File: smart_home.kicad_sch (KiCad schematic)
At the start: 0 parts

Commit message: Complete 4-channel smart home AC relay PCB design
Full KiCad 9 design for a 230V AC 4-channel smart home relay controller:
- ESP32-WROOM-32E + ULN2003A + 4x SANYOU SRD relays
- 4 isolated AC inputs (own L/N/PE + fuse per channel)
- 4 AC outputs (L_switched + N_passthrough per channel)
- HLK-PM01 isolated AC-DC + AMS1117-3.3 LDO for logic
- Per-channel current sense (4x ACS712-05B + ADC dividers)
- Per-channel voltage sense (ADS1115 I2C ADC + external ZMPT101B headers)
- 4-pin I2C header for 16x2 LCD module (PCF8574 backpack)
- Manual override buttons + status LEDs per channel
- 6-pin UART programming header
- Custom DRC: 4mm HV-LV clearance, 3mm HV-HV, 2mm HV trace minimum
- Physical HV/LV isolation slot in PCB

Layout: 200x100mm 2-layer FR4, 76 components, mostly routed (Freerouting).
21 HV channel-internal traces still need manual routing in KiCad.

Includes generator scripts (generate_sch.py, generate_pcb.py, add_acs712.py,
add_voltage_sense.py) that build everything from bom.csv. Fabrication
gerbers + drill + pick-and-place files in fabrication/.
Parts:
- added C1: 100uF/16V, Capacitor_THT:CP_Radial_D6.3mm_P2.50mm, symbol Device:C_Polarized
- added C10, C11, C16, C5, C7, C8, C9: 100nF 0805, Capacitor_SMD:C_0805_2012Metric, symbol Device:C
- added C2, C4: 10uF 0805, Capacitor_SMD:C_0805_2012Metric, symbol Device:C
- added C3: 22uF 0805, Capacitor_SMD:C_0805_2012Metric, symbol Device:C
- added C6: 1uF 0805, Capacitor_SMD:C_0805_2012Metric, symbol Device:C
- added D1, D2, D3, D4: LED 3mm Green, LED_THT:LED_D3.0mm, symbol Device:LED
- added D5: LED 3mm Red, LED_THT:LED_D3.0mm, symbol Device:LED
- added F1, F2, F3, F4: T4A 5x20mm, Fuse:Fuseholder_Cylinder-5x20mm_Schurter_0031_8201_Horizontal_Open, symbol Device:Fuse
- added J1A, J1B, J1C, J1D: Screw terminal 3-pos 5.08mm, TerminalBlock_Phoenix:TerminalBlock_Phoenix_MKDS-1,5-3-5.08_1x03_P5.08mm_Horizontal, symbol Connector_Generic:Conn_01x03
- added J2A, J2B, J2C, J2D: Screw terminal 2-pos 5.08mm, TerminalBlock_Phoenix:TerminalBlock_Phoenix_MKDS-1,5-2-5.08_1x02_P5.08mm_Horizontal, symbol Connector_Generic:Conn_01x02
- added J3: Pin header 1x06 2.54mm, Connector_PinHeader_2.54mm:PinHeader_1x06_P2.54mm_Vertical, symbol Connector_Generic:Conn_01x06
- added J4: Pin header 1x04 2.54mm, Connector_PinHeader_2.54mm:PinHeader_1x04_P2.54mm_Vertical, symbol Connector_Generic:Conn_01x04
- added J5, J6, J7, J8: Pin header 1x03 2.54mm, Connector_PinHeader_2.54mm:PinHeader_1x03_P2.54mm_Vertical, symbol Connector_Generic:Conn_01x03
- added K1, K2, K3, K4: SRD-05VDC-SL-C, Relay_THT:Relay_SPDT_SANYOU_SRD_Series_Form_C, symbol Relay:SANYOU_SRD_Form_C
- added PS1: HLK-PM01, hlk_pm01:HLK-PM01, symbol hlk_pm01:HLK-PM01
- added R1, R2, R3, R4, R9: 1k 0805, Resistor_SMD:R_0805_2012Metric, symbol Device:R
- added R11, R12, R15, R16, R17, R18, R5, R6, R7, R8: 10k 0805, Resistor_SMD:R_0805_2012Metric, symbol Device:R
- added R13, R14: 4.7k 0805, Resistor_SMD:R_0805_2012Metric, symbol Device:R
- added R19, R20, R21, R22: 18k 0805, Resistor_SMD:R_0805_2012Metric, symbol Device:R
- added RV1: S07K275, Varistor:RV_Disc_D9mm_W5.2mm_P5mm, symbol Device:Varistor
- added SW1, SW2, SW3, SW4, SW5, SW6: 6mm tactile, Button_Switch_THT:SW_PUSH_6mm, symbol Switch:SW_Push
- added U1: ESP32-WROOM-32E, RF_Module:ESP32-WROOM-32, symbol RF_Module:ESP32-WROOM-32E
- added U2: ULN2003A, Package_DIP:DIP-16_W7.62mm, symbol Transistor_Array:ULN2003A
- added U3: AMS1117-3.3, Package_TO_SOT_SMD:SOT-223-3_TabPin2, symbol Regulator_Linear:AMS1117-3.3
- added U4, U5, U6, U7: ACS712-05B, Package_SO:SOIC-8_3.9x4.9mm_P1.27mm, symbol Sensor_Current:ACS712xLCTR-05B
- added U8: ADS1115, Package_SO:TSSOP-10_3x3mm_P0.5mm, symbol Analog_ADC:ADS1115IDGS
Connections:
- new net: U1.1 (GND), U1.15 (GND), U1.38 (GND), U1.39 (GND)
- new net: U4.1 (IP+), U4.2 (IP+)
- new net: U4.3 (IP-), U4.4 (IP-)
- new net: U6.1 (IP+), U6.2 (IP+)
- new net: U6.3 (IP-), U6.4 (IP-)
- new net: U7.1 (IP+), U7.2 (IP+)
- new net: U7.3 (IP-), U7.4 (IP-)
- new net: U5.1 (IP+), U5.2 (IP+)
- new net: U5.3 (IP-), U5.4 (IP-)

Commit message: Add full component details to README and company name to PCB
- Update company in title block: Wisright -> WisRight Technologies Private Limited
  (smart_home.kicad_sch, smart_home.kicad_pcb, generate_sch.py)
- Add silkscreen on PCB:
  * Front silk (bottom center): "WisRight Technologies Private Limited" (bold 1.4mm)
  * Back silk (top, mirrored): "Smart Home 4-Channel AC Relay Controller - Rev 0.1"
  * Back silk (bottom, mirrored): "(c) 2026 WisRight Technologies Pvt Ltd"
- Expand README with detailed components list (active devices, passives,
  switches, connectors, external modules, custom lib parts)
- Add LICENSE file (MIT with WisRight copyright)
- Regenerate fabrication gerbers with updated silkscreen
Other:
- company: Wisright -> WisRight Technologies Private Limited
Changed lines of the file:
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@@
 		(date "2026-05-26")
 		(rev "0.1")
-		(company "Wisright")
+		(company "WisRight Technologies Private Limited")
 		(comment 1 "ESP32-WROOM-32E + HLK-PM01 + 4x SRD-05VDC relays")
 		(comment 2 "230VAC input, 4 switched AC load outputs, UART programming header")

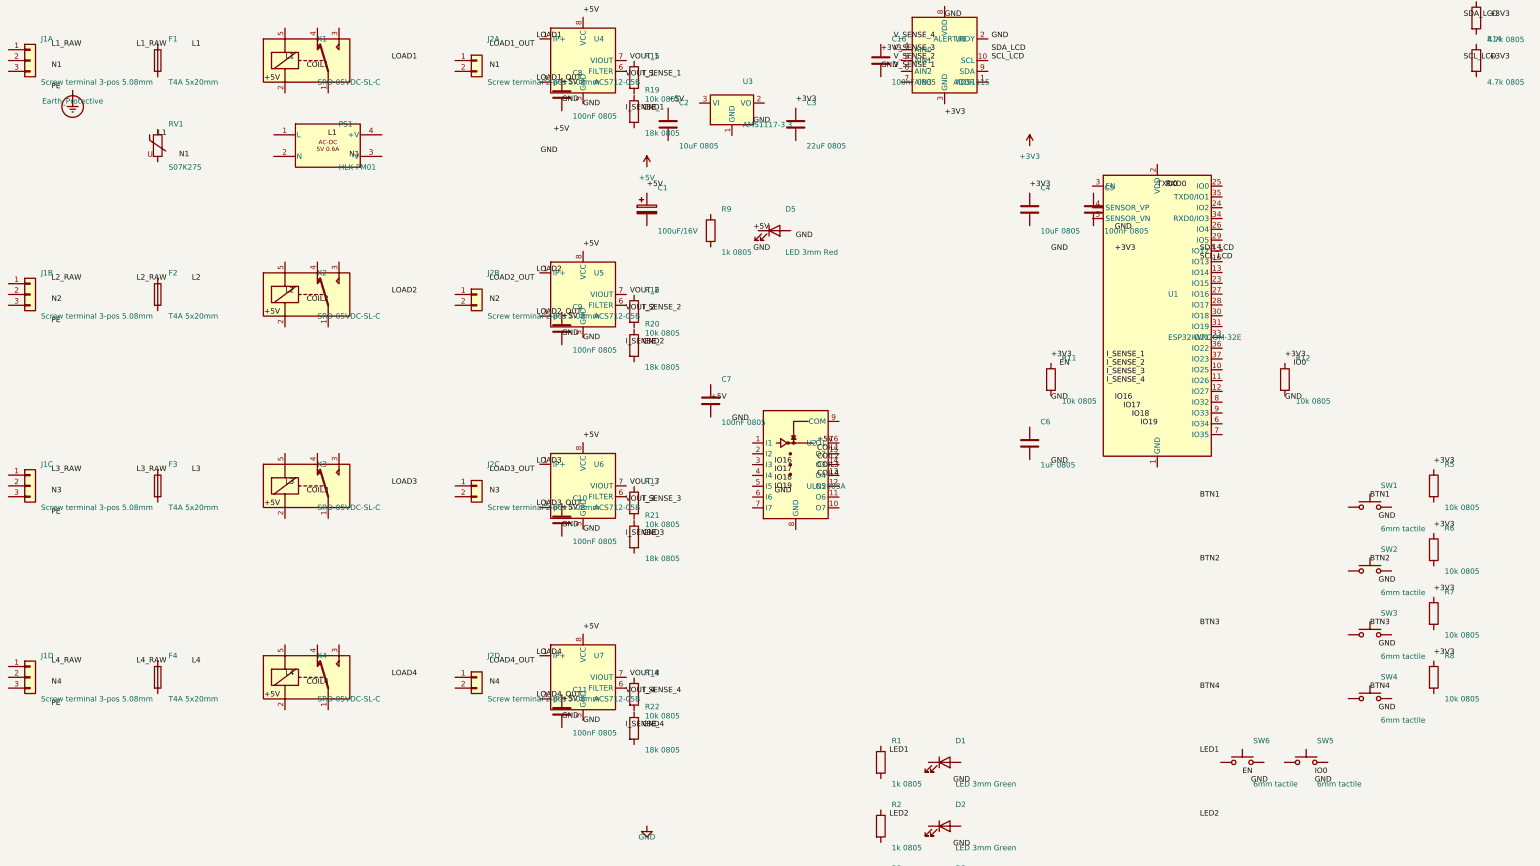
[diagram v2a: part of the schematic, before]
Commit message: Expand BOM with manufacturer parts, sourcing notes, external modules
bom.csv:
- Add manufacturer names (Espressif, TI, Allegro, Phoenix Contact, etc.)
- Add specific MPNs for sourcing (Yageo / Samsung MLCC / Schurter fuse holder)
- Properly quote J1A-J1D and J2A-J2D footprint fields (the unquoted commas
  in MKDS-1,5 part names were a CSV parsing hazard)
- More descriptive Notes per part (placement guidance, alternatives, ratings)
- New #EXTERNAL section listing modules NOT on the PCB:
  * LCD1 — 16x2 LCD with PCF8574 I2C backpack (to J4)
  * VS1-VS4 — ZMPT101B voltage sensor modules (to J5-J8)
  * USB1 — USB-to-Serial adapter (to J3, programming only)

generate_sch.py:
- load_bom() now skips rows starting with '#' (comments) and rows with
  empty KiCad Symbol field (external modules), so the new bom.csv format
  still produces the expected 43 PCB-mounted BOM rows / 76 components.
- Remove a stray 'from __future__ import' line with no module name
  (syntax error that pre-existed but went undetected).
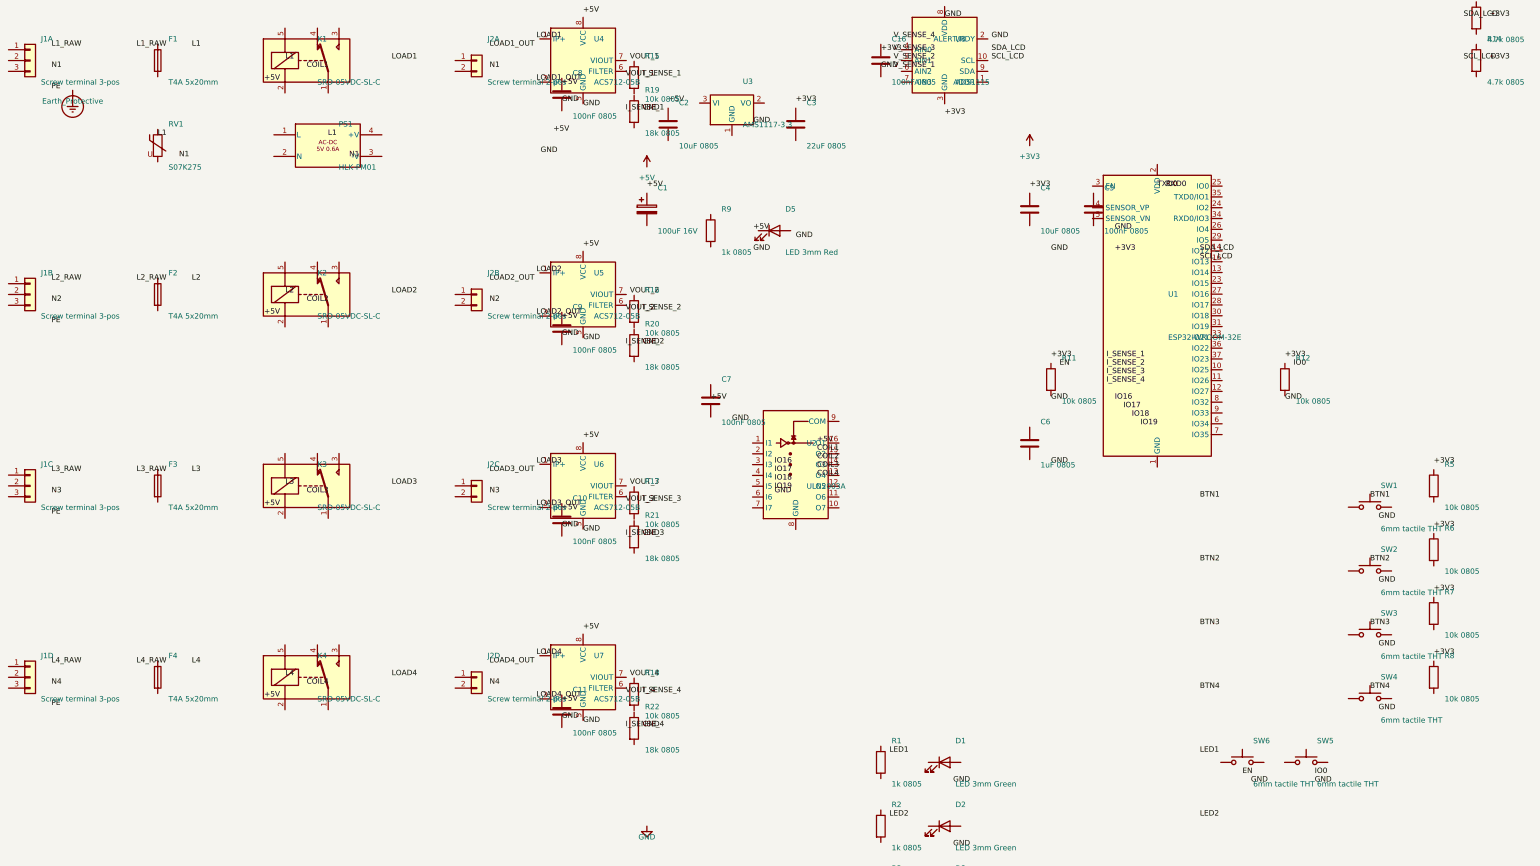
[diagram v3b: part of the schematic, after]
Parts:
- C1: value 100uF/16V -> 100uF 16V
- J1A, J1B, J1C, J1D: value Screw terminal 3-pos 5.08mm -> Screw terminal 3-pos
- J2A, J2B, J2C, J2D: value Screw terminal 2-pos 5.08mm -> Screw terminal 2-pos
- SW1, SW2, SW3, SW4, SW5, SW6: value 6mm tactile -> 6mm tactile THT
